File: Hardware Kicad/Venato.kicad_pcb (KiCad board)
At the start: 2 copper layers, 84 x 35.3 mm, 24 parts, among them J1 Conn_01x02_Male, J2 Conn_01x02_Male, J3 Conn_01x02_Male, J4 Conn_01x02_Male, J5 Conn_01x02_Male, J6 Conn_01x02_Male, J7 Conn_01x05_Male, U1 LM317_TO-220, U2 MCP6002-xP, U3 MCP6002-xP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

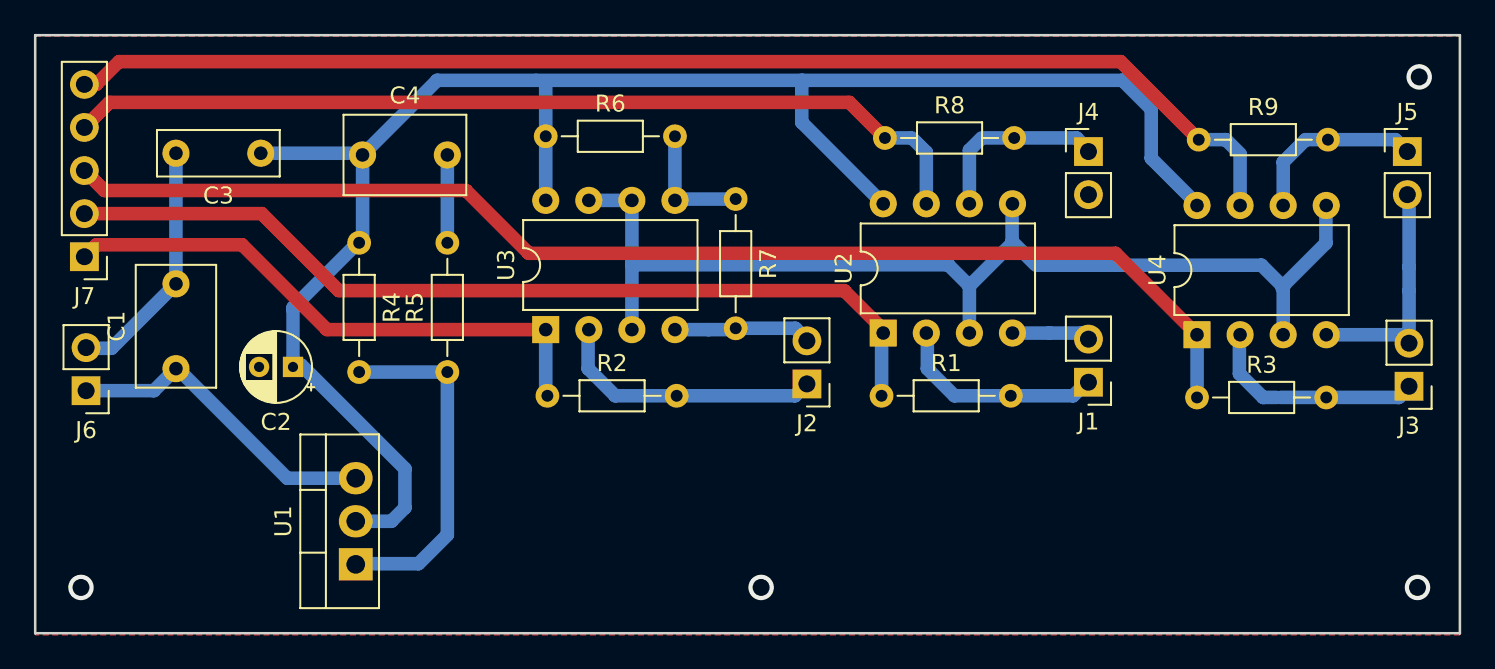
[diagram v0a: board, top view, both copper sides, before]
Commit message: 1mm traces and fix resistor
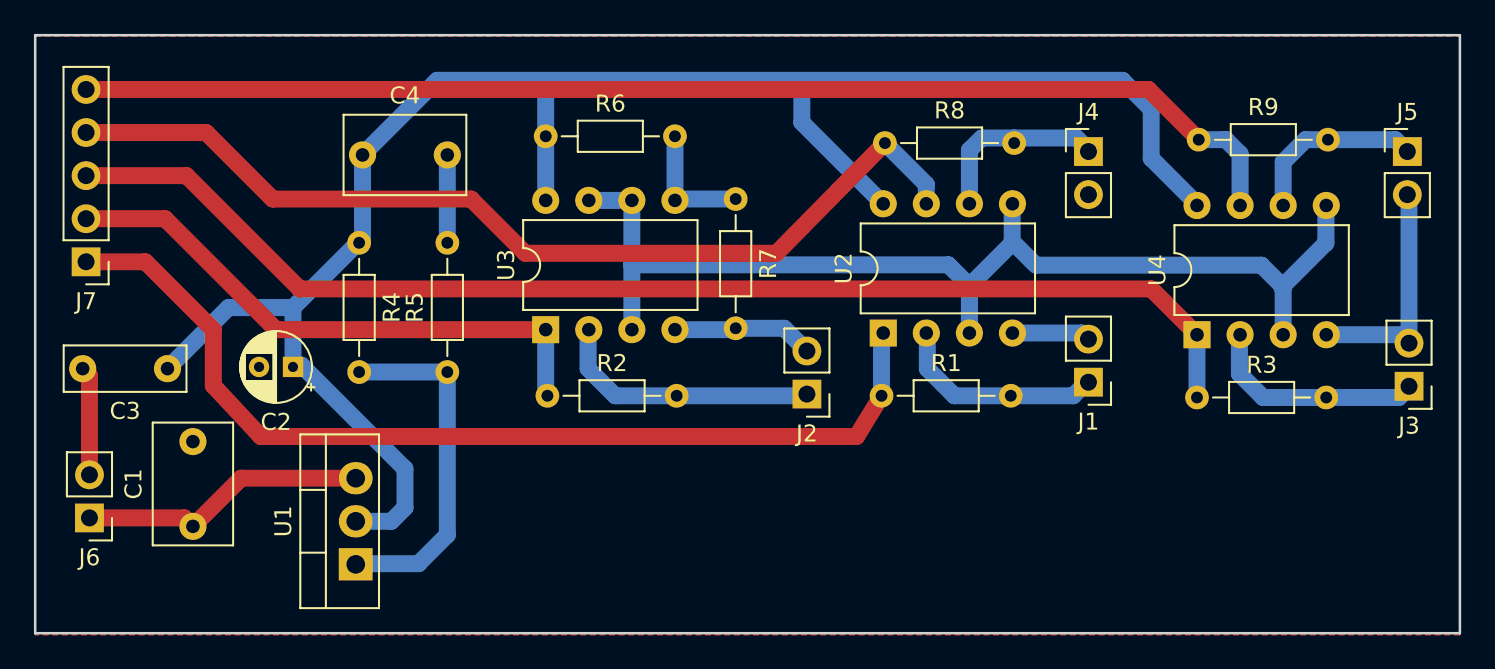
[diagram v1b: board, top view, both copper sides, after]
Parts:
- R7: value 9k -> 3k
- moved C3 13.8 mm to (20.8, 32.6)
- moved C1 9.35 mm to (22.3, 41.9)
- moved J6 7.50 mm to (16.2, 41.4)
- moved J2 0.60 mm to (58.5, 34.1)
- moved J7 0.32 mm to (16.0, 26.3)
- moved R8 0.30 mm to (63.1, 19.3)
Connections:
- J7 pad 1: SENSE2 -> SENSE1
- J7 pad 2: SENSE1 -> SENSE2
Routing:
- net GND: track 46.9 -> 38.8 mm
- net SENSE1: track 53.4 -> 58.2 mm
- net +3.3VA: track 106.7 -> 109.7 mm
- net SENSE5: track 54.4 -> 57.4 mm
- net +5V: track 19.2 -> 17.1 mm
- net SENSE3: track 74.0 -> 72.8 mm
- net Net-(J2-Pad1): track 16.3 -> 15.2 mm
- net (no net): vias 4 -> 0
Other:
- net class Default: trace_width 0.25 -> 0.5
